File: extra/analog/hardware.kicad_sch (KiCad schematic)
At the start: 12 parts, among them J1 Screw_Terminal_01x05, J2 RFShield_OnePiece, J4 Conn_01x04_Socket, J6 RFShield_OnePiece, J7 Conn_01x04_Socket

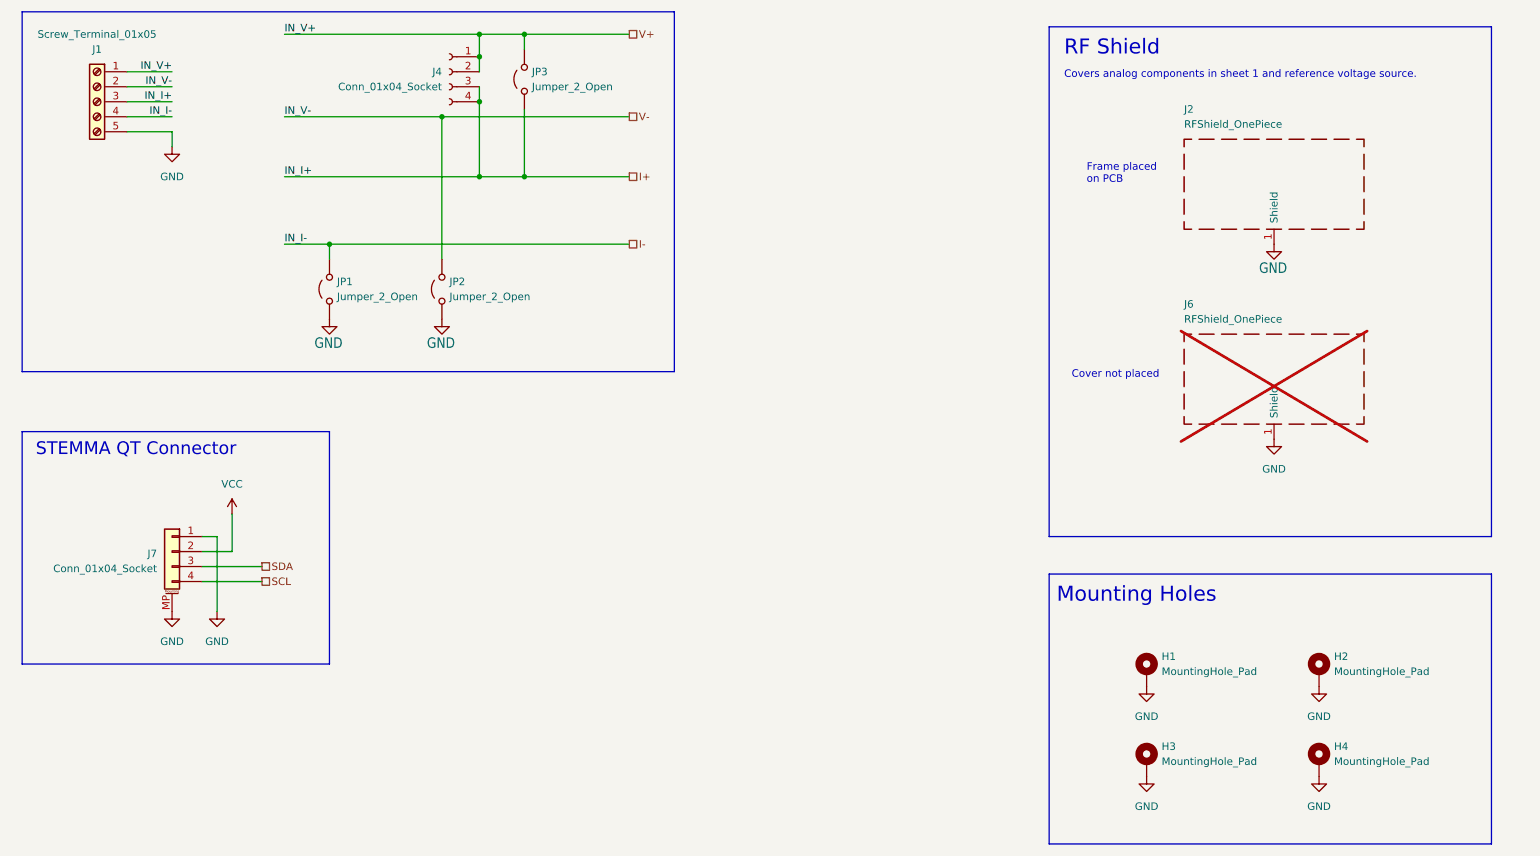
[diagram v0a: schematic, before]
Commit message: Added component values
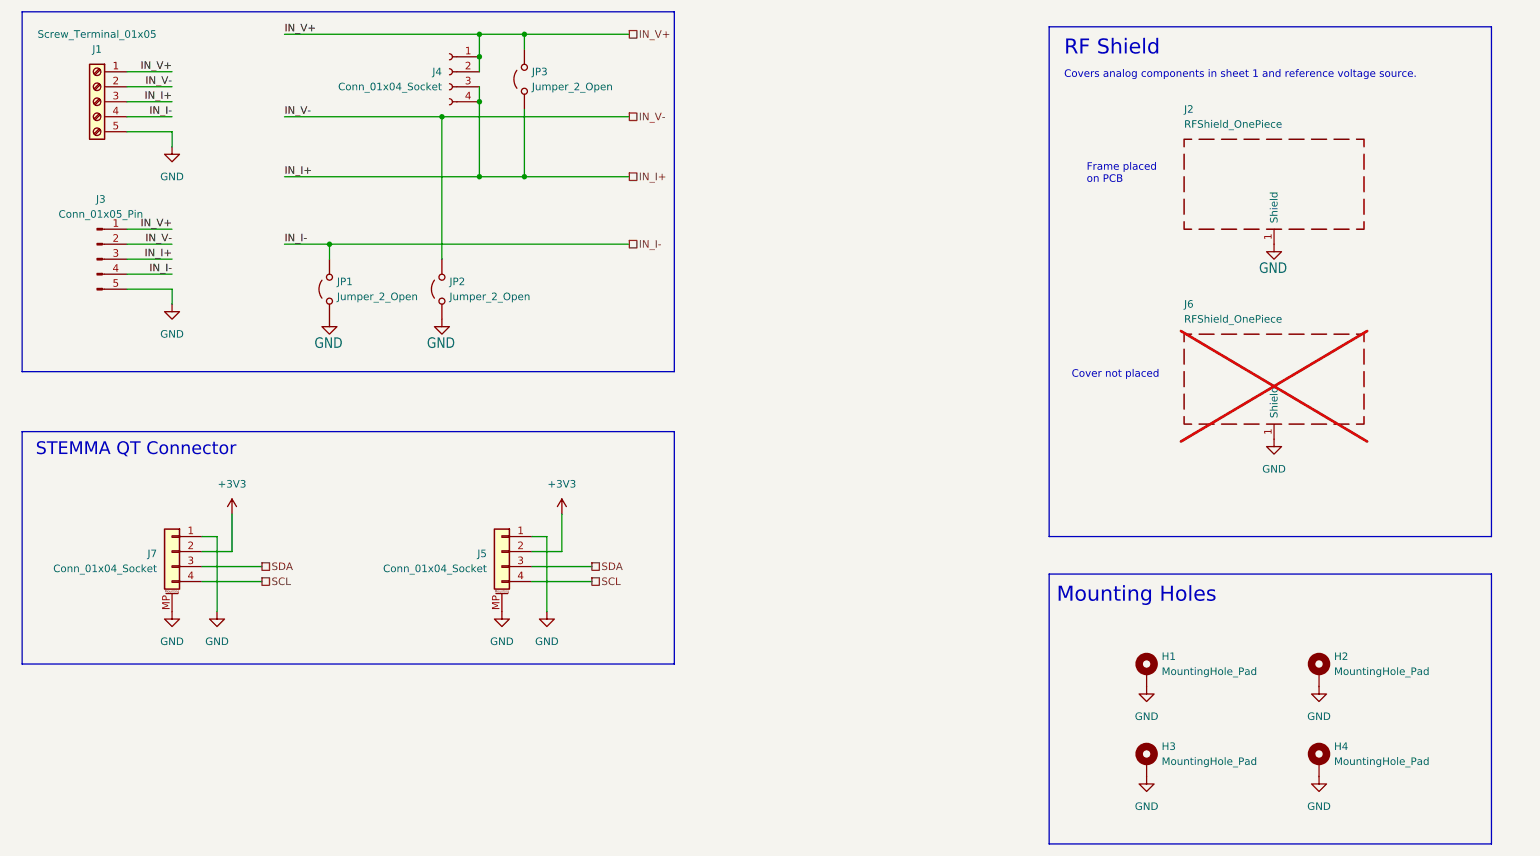
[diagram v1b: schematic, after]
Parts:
- added J3: Conn_01x05_Pin, Connector_PinHeader_2.54mm:PinHeader_1x05_P2.54mm_Vertical, symbol Connector:Conn_01x05_Pin
- added J5: Conn_01x04_Socket, Connector_JST:JST_SH_SM04B-SRSS-TB_1x04-1MP_P1.00mm_Horizontal, symbol Connector_Generic_MountingPin:Conn_01x04_MountingPin
- H1, H2, H3, H4: now in the parts list
- J4: footprint (none) -> Connector_PinSocket_2.54mm:PinSocket_1x04_P2.54mm_Vertical
- JP1, JP2, JP3: footprint (none) -> Connector_PinHeader_1.00mm:PinHeader_1x02_P1.00mm_Vertical
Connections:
- net GND: now also J3.5 (Pin_5), J5.1 (Pin_1), J5.MP (MountPin)
- net SCL: now also J5.4 (Pin_4)
- net SDA: now also J5.3 (Pin_3)
- net I+ renamed IN_I+
- net IN_I+: now also J3.3 (Pin_3)
- net I- renamed IN_I-
- net IN_I-: now also J3.4 (Pin_4)
- net V+ renamed IN_V+
- net IN_V+: now also J3.1 (Pin_1)
- net V- renamed IN_V-
- net IN_V-: now also J3.2 (Pin_2)
- net VCC renamed +3V3
- net +3V3: now also J5.2 (Pin_2)

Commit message: Placed and routed components
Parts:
- JP1, JP2, JP3: footprint Connector_PinHeader_1.00mm:PinHeader_1x02_P1.00mm_Vertical -> Connector_PinHeader_2.54mm:PinHeader_1x02_P2.54mm_Vertical
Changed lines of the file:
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@@
 			)
 		)
-		(property "Footprint" "Connector_PinHeader_1.00mm:PinHeader_1x02_P1.00mm_Vertical"
+		(property "Footprint" "Connector_PinHeader_2.54mm:PinHeader_1x02_P2.54mm_Vertical"
 			(at 80.01 63.5 0)
 			(effects
@@
 			)
 		)
-		(property "Footprint" "Connector_PinHeader_1.00mm:PinHeader_1x02_P1.00mm_Vertical"
+		(property "Footprint" "Connector_PinHeader_2.54mm:PinHeader_1x02_P2.54mm_Vertical"
 			(at 99.06 63.5 0)
 			(effects
@@
 			)
 		)
-		(property "Footprint" "Connector_PinHeader_1.00mm:PinHeader_1x02_P1.00mm_Vertical"
+		(property "Footprint" "Connector_PinHeader_2.54mm:PinHeader_1x02_P2.54mm_Vertical"
 			(at 113.03 27.94 0)
 			(effects

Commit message: Finalization with jack
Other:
- company: (none) -> jlab
- title: (none) -> Analog Frontend
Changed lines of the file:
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@@
 	(generator_version "9.0")
 	(paper "A4")
+	(title_block
+		(title "Analog Frontend")
+		(date "2026-03-13")
+		(rev "v3.0.0")
+		(company "jlab")
+	)
 	(rectangle
 		(start 201.93 111.76)
@@
 	)
 	(junction
+		(at 60.96 116.84)
+		(diameter 0)
+		(color 0 0 0 0)
+	)
+	(junction
 		(at 113.03 20.32)
+		(diameter 0)
+		(color 0 0 0 0)
+	)
+	(junction
+		(at 63.5 107.95)
 		(diameter 0)
 		(color 0 0 0 0)
@@
 	(wire
 		(pts
-			(xy 60.96 105.41) (xy 60.96 118.11)
+			(xy 60.96 105.41) (xy 60.96 116.84)
+		)
+		(stroke
+			(width 0)
+			(type default)
+		)
+	)
+	(wire
+		(pts
+			(xy 60.96 116.84) (xy 80.01 116.84)
 		)
 		(stroke
@@
 	(wire
 		(pts
+			(xy 60.96 116.84) (xy 60.96 118.11)
+		)
+		(stroke
+			(width 0)
+			(type default)
+		)
+	)
+	(wire
+		(pts
 			(xy 45.72 53.34) (xy 53.34 53.34)
 		)
@@
 		(pts
 			(xy 105.41 24.13) (xy 105.41 26.67)
+		)
+		(stroke
+			(width 0)
+			(type default)
+		)
+	)
+	(wire
+		(pts
+			(xy 63.5 107.95) (xy 71.12 107.95)
 		)
 		(stroke
@@
 					(unit 1)
 				)
+			)
+		)
+	)
+	(symbol
+		(lib_id "power:PWR_FLAG")
+		(at 71.12 107.95 0)
+		(unit 1)
+		(exclude_from_sim no)
+		(in_bom yes)
+		(on_board yes)
+		(dnp no)
+		(fields_autoplaced yes)
+		(property "Reference" "#FLG01"
+			(at 71.12 106.045 0)
+			(effects
+				(font
+					(size 1.27 1.27)
+				)
+				(hide yes)
+			)
+		)
+		(property "Value" "PWR_FLAG"
+			(at 71.12 102.87 0)
+			(effects
+				(font
+					(size 1.27 1.27)
+				)
+			)
+		)
+		(property "Footprint" ""
+			(at 71.12 107.95 0)
+			(effects
+				(font
+					(size 1.27 1.27)
+				)
+				(hide yes)
+			)
+		)
+		(property "Datasheet" "~"
+			(at 71.12 107.95 0)
+			(effects
+				(font
+					(size 1.27 1.27)
+				)
+				(hide yes)
+			)
+		)
+		(property "Description" "Special symbol for telling ERC where power comes from"
+			(at 71.12 107.95 0)
+			(effects
+				(font
+					(size 1.27 1.27)
+				)
+				(hide yes)
+			)
+		)
+		(pin "1"
+		)
+		(instances
+			(project "analog"
+				(path "/23b89991-5554-4fb2-a43f-c8e9c24413b6/44929bcc-8b4b-4f87-8f85-3fe7cd185de8"
+					(reference "#FLG01")
+					(unit 1)
+				)
+			)
+		)
+	)
+	(symbol
+		(lib_id "power:PWR_FLAG")
+		(at 80.01 116.84 0)
+		(unit 1)
+		(exclude_from_sim no)
+		(in_bom yes)
+		(on_board yes)
+		(dnp no)
+		(fields_autoplaced yes)
+		(property "Reference" "#FLG02"
+			(at 80.01 114.935 0)
+			(effects
+				(font
+					(size 1.27 1.27)
+				)
+				(hide yes)
+			)
+		)
+		(property "Value" "PWR_FLAG"
+			(at 80.01 111.76 0)
+			(effects
+				(font
+					(size 1.27 1.27)
+				)
+			)
+		)
+		(property "Footprint" ""
+			(at 80.01 116.84 0)
+			(effects
+				(font
+					(size 1.27 1.27)
+				)
+				(hide yes)
+			)
+		)
+		(property "Datasheet" "~"
+			(at 80.01 116.84 0)
+			(effects
+				(font
+					(size 1.27 1.27)
+				)
+				(hide yes)
+			)
+		)
+		(property "Description" "Special symbol for telling ERC where power comes from"
+			(at 80.01 116.84 0)
+			(effects
+				(font
+					(size 1.27 1.27)
+				)
+				(hide yes)
+			)
+		)
+		(pin "1"
+		)
+		(instances
+			(project "analog"
+				(path "/23b89991-5554-4fb2-a43f-c8e9c24413b6/44929bcc-8b4b-4f87-8f85-3fe7cd185de8"
+					(reference "#FLG02")
+					(unit 1)
+				)

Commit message: Generated production files
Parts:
- H1, H2, H3, H4, J1, J3, J4, JP1, JP2, JP3: now left out of the parts list
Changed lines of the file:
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@@
 	(title_block
 		(title "Analog Frontend")
-		(date "2026-03-13")
-		(rev "v3.0.0")
+		(date "2026-04-06")
+		(rev "v3.1.0")
 		(company "jlab")
 	)
@@
 		(unit 1)
 		(exclude_from_sim no)
-		(in_bom yes)
+		(in_bom no)
 		(on_board yes)
 		(dnp no)
@@
 		(unit 1)
 		(exclude_from_sim no)
-		(in_bom yes)
+		(in_bom no)
 		(on_board yes)
 		(dnp no)
@@
 		(unit 1)
 		(exclude_from_sim no)
-		(in_bom yes)
+		(in_bom no)
 		(on_board yes)
 		(dnp no)
@@
 		(unit 1)
 		(exclude_from_sim no)
-		(in_bom yes)
+		(in_bom no)
 		(on_board yes)
 		(dnp no)
@@
 		(unit 1)
 		(exclude_from_sim no)
-		(in_bom yes)
+		(in_bom no)
 		(on_board yes)
 		(dnp no)
@@
 		(unit 1)
 		(exclude_from_sim no)
-		(in_bom yes)
+		(in_bom no)
 		(on_board yes)
 		(dnp no)
@@
 		(unit 1)
 		(exclude_from_sim no)
-		(in_bom yes)
+		(in_bom no)
 		(on_board yes)
 		(dnp no)
@@
 		(unit 1)
 		(exclude_from_sim no)
-		(in_bom yes)
+		(in_bom no)
 		(on_board yes)
 		(dnp no)
@@
 		(unit 1)
 		(exclude_from_sim no)
-		(in_bom yes)
+		(in_bom no)
 		(on_board yes)
 		(dnp no)
@@
 		(unit 1)
 		(exclude_from_sim no)
-		(in_bom yes)
+		(in_bom no)
 		(on_board yes)
 		(dnp no)
